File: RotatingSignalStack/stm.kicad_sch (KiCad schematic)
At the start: 17 parts, among them IC2 STM32H562RIT6, J2 Conn_01x04, SW1 SW_Push, SW2 Boot Switch

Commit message: more layout
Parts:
- C12, C13, C19, C20, C30, C31, C32, C33, C34, C35, C4: footprint Capacitor_SMD:C_0603_1608Metric_Pad1.08x0.95mm_HandSolder -> Capacitor_SMD:C_0402_1005Metric_Pad0.74x0.62mm_HandSolder
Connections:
- net VCAP1: no longer C32.2, IC2.62 (VCAP_2)
- new net VCAP2: C32.2, IC2.62 (VCAP_2)
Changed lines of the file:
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@@
 	)
 	(junction
-		(at 140.97 24.13)
-		(diameter 0)
-		(color 0 0 0 0)
-	)
-	(junction
 		(at 209.55 49.53)
 		(diameter 0)
@@
 	)
 	(junction
-		(at 140.97 27.94)
-		(diameter 0)
-		(color 0 0 0 0)
-	)
-	(junction
 		(at 238.76 49.53)
 		(diameter 0)
@@
 	(wire
 		(pts
-			(xy 140.97 24.13) (xy 140.97 27.94)
+			(xy 140.97 24.13) (xy 140.97 33.02)
 		)
 		(stroke
@@
 	(wire
 		(pts
-			(xy 154.94 27.94) (xy 140.97 27.94)
-		)
-		(stroke
-			(width 0)
-			(type default)
-		)
-	)
-	(wire
-		(pts
 			(xy 36.83 129.54) (xy 59.69 129.54)
 		)
@@
 	(wire
 		(pts
+			(xy 96.52 144.78) (xy 96.52 154.94)
+		)
+		(stroke
+			(width 0)
+			(type default)
+		)
+	)
+	(wire
+		(pts
 			(xy 208.28 27.94) (xy 209.55 27.94)
 		)
@@
 	(wire
 		(pts
-			(xy 140.97 20.32) (xy 140.97 24.13)
-		)
-		(stroke
-			(width 0)
-			(type default)
-		)
-	)
-	(wire
-		(pts
 			(xy 198.12 96.52) (xy 200.66 96.52)
 		)
@@
 	(wire
 		(pts
-			(xy 140.97 27.94) (xy 140.97 33.02)
-		)
-		(stroke
-			(width 0)
-			(type default)
-		)
-	)
-	(wire
-		(pts
-			(xy 140.97 20.32) (xy 137.16 20.32)
+			(xy 137.16 20.32) (xy 154.94 20.32)
 		)
 		(stroke
@@
 	(wire
 		(pts
-			(xy 154.94 33.02) (xy 154.94 27.94)
+			(xy 154.94 20.32) (xy 154.94 33.02)
 		)
 		(stroke
@@
 		)
 	)
-	(global_label "VSS_1"
-		(shape bidirectional)
-		(at 96.52 144.78 270)
-		(fields_autoplaced yes)
-		(effects
-			(font
-				(size 1.27 1.27)
-			)
-			(justify right)
-		)
-		(property "Intersheetrefs" "${INTERSHEET_REFS}"
-			(at 96.52 154.5612 90)
-			(effects
-				(font
-					(size 1.27 1.27)
-				)
-				(justify right)
-				(hide yes)
-			)
-		)
-	)
 	(global_label "VSS_2"
 		(shape bidirectional)
@@
 			)
 		)
-		(property "Footprint" "Capacitor_SMD:C_0603_1608Metric_Pad1.08x0.95mm_HandSolder"
+		(property "Footprint" "Capacitor_SMD:C_0402_1005Metric_Pad0.74x0.62mm_HandSolder"
 			(at 252.4252 81.28 0)
 			(effects
@@
 			)
 		)
-		(property "Footprint" "Capacitor_SMD:C_0603_1608Metric_Pad1.08x0.95mm_HandSolder"
+		(property "Footprint" "Capacitor_SMD:C_0402_1005Metric_Pad0.74x0.62mm_HandSolder"
 			(at 267.6652 110.49 0)
 			(effects
@@
 			)
 		)
-		(property "Footprint" "Capacitor_SMD:C_0603_1608Metric_Pad1.08x0.95mm_HandSolder"
+		(property "Footprint" "Capacitor_SMD:C_0402_1005Metric_Pad0.74x0.62mm_HandSolder"
 			(at 267.6652 81.28 0)
 			(effects
@@
 			)
 		)
-		(property "Footprint" "Capacitor_SMD:C_0603_1608Metric_Pad1.08x0.95mm_HandSolder"
+		(property "Footprint" "Capacitor_SMD:C_0402_1005Metric_Pad0.74x0.62mm_HandSolder"
 			(at 140.0048 33.02 0)
 			(effects
@@
 			)
 		)
-		(property "Footprint" "Capacitor_SMD:C_0603_1608Metric_Pad1.08x0.95mm_HandSolder"
+		(property "Footprint" "Capacitor_SMD:C_0402_1005Metric_Pad0.74x0.62mm_HandSolder"
 			(at 25.0952 124.46 0)
 			(effects
@@
 			)
 		)
-		(property "Footprint" "Capacitor_SMD:C_0603_1608Metric_Pad1.08x0.95mm_HandSolder"
+		(property "Footprint" "Capacitor_SMD:C_0402_1005Metric_Pad0.74x0.62mm_HandSolder"
 			(at 225.7552 45.72 0)
 			(effects
@@
 			)
 		)
-		(property "Footprint" "Capacitor_SMD:C_0603_1608Metric_Pad1.08x0.95mm_HandSolder"
+		(property "Footprint" "Capacitor_SMD:C_0402_1005Metric_Pad0.74x0.62mm_HandSolder"
 			(at 267.6652 45.72 0)
 			(effects
@@
 	(symbol
 		(lib_id "power:GND")
+		(at 96.52 154.94 0)
+		(unit 1)
+		(exclude_from_sim no)
+		(in_bom yes)
+		(on_board yes)
+		(dnp no)
+		(fields_autoplaced yes)
+		(property "Reference" "#PWR026"
+			(at 96.52 161.29 0)
+			(effects
+				(font
+					(size 1.27 1.27)
+				)
+				(hide yes)
+			)
+		)
+		(property "Value" "GND"
+			(at 96.52 160.02 0)
+			(effects
+				(font
+					(size 1.27 1.27)
+				)
+			)
+		)
+		(property "Footprint" ""
+			(at 96.52 154.94 0)
+			(effects
+				(font
+					(size 1.27 1.27)
+				)
+				(hide yes)
+			)
+		)
+		(property "Datasheet" ""
+			(at 96.52 154.94 0)
+			(effects
+				(font
+					(size 1.27 1.27)
+				)
+				(hide yes)
+			)
+		)
+		(property "Description" "Power symbol creates a global label with name \"GND\" , ground"
+			(at 96.52 154.94 0)
+			(effects
+				(font
+					(size 1.27 1.27)
+				)
+				(hide yes)
+			)
+		)
+		(pin "1"
+		)
+		(instances
+			(project ""
+				(path "/fbbbfa89-3c28-4cf8-856b-66ca7308742c/85f5c4be-2744-4dc6-8792-10e4391fb2cb"
+					(reference "#PWR026")
+					(unit 1)
+				)
+			)
+		)
+	)
+	(symbol
+		(lib_id "power:GND")
 		(at 181.61 38.1 0)
 		(unit 1)
@@
 			)
 		)
-		(property "Footprint" "Capacitor_SMD:C_0603_1608Metric_Pad1.08x0.95mm_HandSolder"
+		(property "Footprint" "Capacitor_SMD:C_0402_1005Metric_Pad0.74x0.62mm_HandSolder"
 			(at 253.6952 45.72 0)
 			(effects
@@
 			)
 		)
-		(property "Footprint" "Capacitor_SMD:C_0603_1608Metric_Pad1.08x0.95mm_HandSolder"
+		(property "Footprint" "Capacitor_SMD:C_0402_1005Metric_Pad0.74x0.62mm_HandSolder"
 			(at 210.5152 45.72 0)
 			(effects
@@
 			)
 		)
-		(property "Footprint" "Capacitor_SMD:C_0603_1608Metric_Pad1.08x0.95mm_HandSolder"
+		(property "Footprint" "Capacitor_SMD:C_0402_1005Metric_Pad0.74x0.62mm_HandSolder"
 			(at 239.7252 45.72 0)
 			(effects
@@
 			)
 		)
-		(property "Footprint" "Capacitor_SMD:C_0603_1608Metric_Pad1.08x0.95mm_HandSolder"
+		(property "Footprint" "Capacitor_SMD:C_0402_1005Metric_Pad0.74x0.62mm_HandSolder"
 			(at 153.9748 33.02 0)
 			(effects

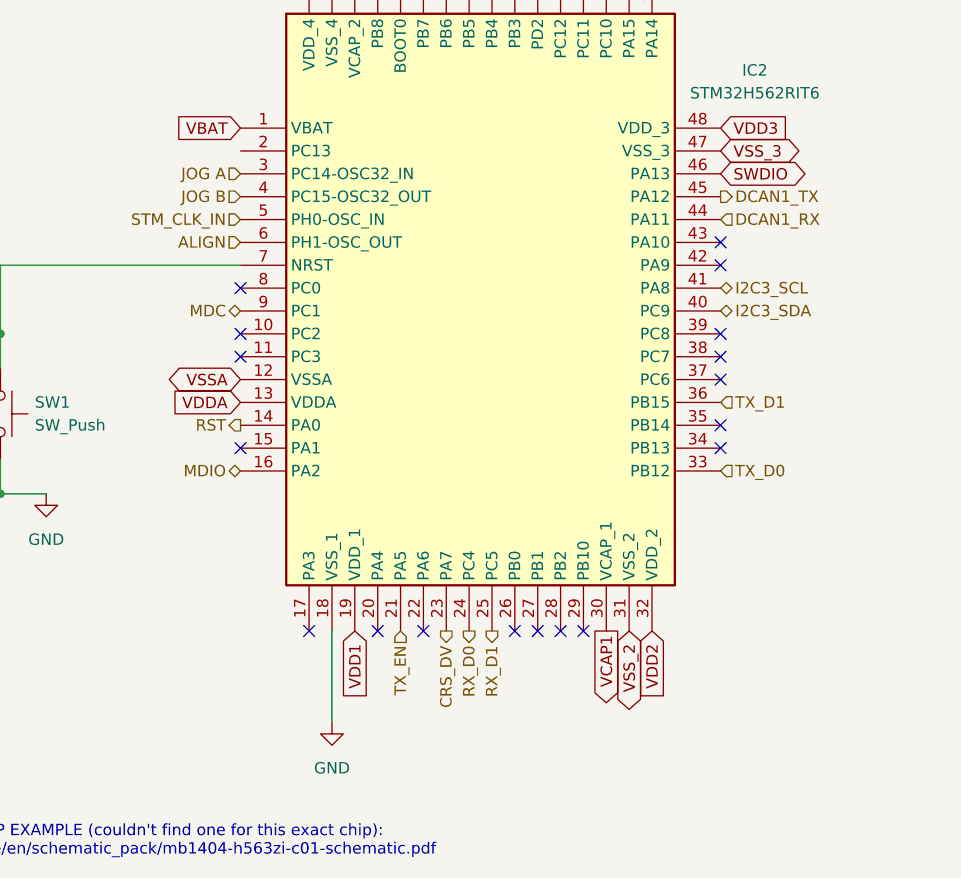
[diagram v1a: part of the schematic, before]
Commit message: Finished traces, added silkscreen
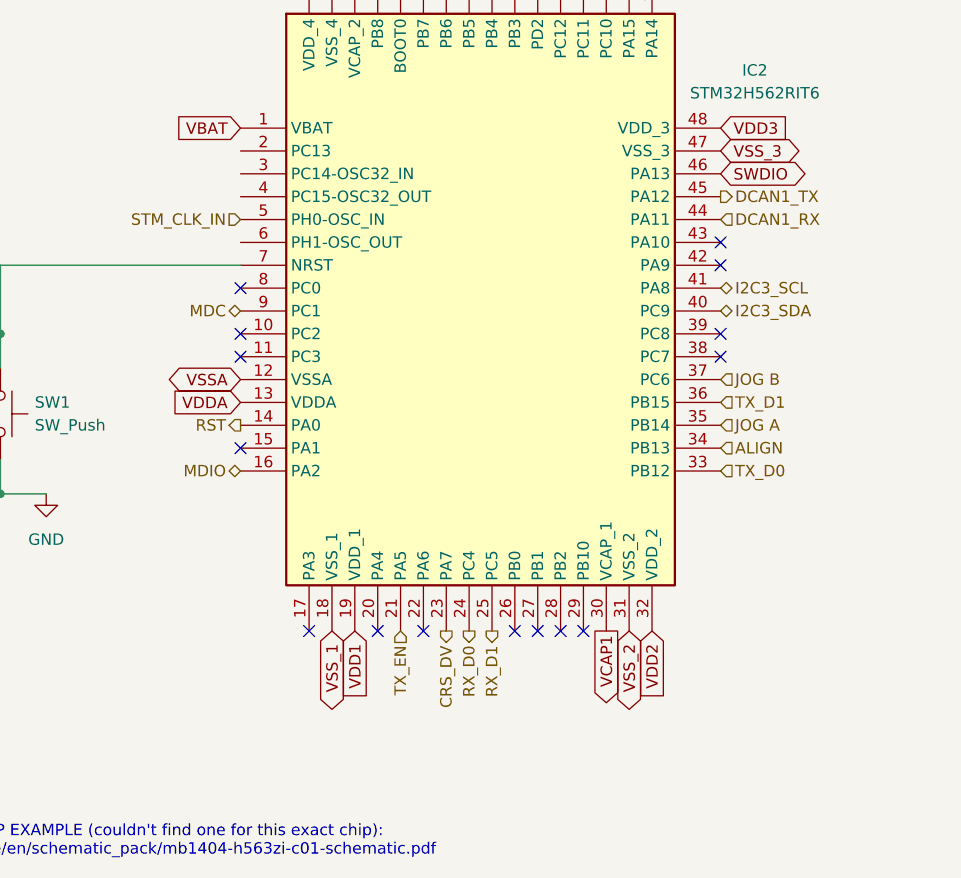
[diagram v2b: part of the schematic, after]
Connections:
- net ALIGN: now also IC2.34 (PB13); no longer IC2.6 (PH1-OSC_OUT)
- net JOG A: now also IC2.35 (PB14); no longer IC2.3 (PC14-OSC32_IN)
- net JOG B: now also IC2.37 (PC6); no longer IC2.4 (PC15-OSC32_OUT)
- no-connect marks 26 -> 23
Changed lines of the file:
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@@
-	)
-	(no_connect
-		(at 139.7 116.84)
 	)
 	(no_connect
@@
 	)
 	(no_connect
-		(at 139.7 121.92)
-	)
-	(no_connect
 		(at 116.84 144.78)
 	)
@@
 		(at 129.54 71.12)
 	)
-	(no_connect
-		(at 139.7 124.46)
-	)
 	(wire
 		(pts
@@
 		(pts
 			(xy 208.28 31.75) (xy 209.55 31.75)
-		)
-		(stroke
-			(width 0)
-			(type default)
-		)
-	)
-	(wire
-		(pts
-			(xy 96.52 144.78) (xy 96.52 154.94)
 		)
 		(stroke
@@
 		)
 	)
+	(global_label "VSS_1"
+		(shape bidirectional)
+		(at 96.52 144.78 270)
+		(fields_autoplaced yes)
+		(effects
+			(font
+				(size 1.27 1.27)
+			)
+			(justify right)
+		)
+		(property "Intersheetrefs" "${INTERSHEET_REFS}"
+			(at 96.52 154.5612 90)
+			(effects
+				(font
+					(size 1.27 1.27)
+				)
+				(justify right)
+				(hide yes)
+			)
+		)
+	)
 	(global_label "SWDIO"
 		(shape bidirectional)
@@
 		)
 	)
-	(hierarchical_label "ALIGN"
+	(hierarchical_label "JOG A"
 		(shape input)
-		(at 86.36 101.6 180)
-		(effects
-			(font
-				(size 1.27 1.27)
-			)
-			(justify right)
+		(at 139.7 121.92 0)
+		(effects
+			(font
+				(size 1.27 1.27)
+			)
+			(justify left)
 		)
 	)
@@
 		)
 	)
+	(hierarchical_label "JOG B"
+		(shape input)
+		(at 139.7 116.84 0)
+		(effects
+			(font
+				(size 1.27 1.27)
+			)
+			(justify left)
+		)
+	)
 	(hierarchical_label "I2C3_SCL"
 		(shape bidirectional)
@@
 		)
 	)
-	(hierarchical_label "JOG A"
+	(hierarchical_label "ALIGN"
 		(shape input)
-		(at 86.36 93.98 180)
-		(effects
-			(font
-				(size 1.27 1.27)
-			)
-			(justify right)
+		(at 139.7 124.46 0)
+		(effects
+			(font
+				(size 1.27 1.27)
+			)
+			(justify left)
 		)
 	)
@@
 		(shape bidirectional)
 		(at 86.36 127 180)
-		(effects
-			(font
-				(size 1.27 1.27)
-			)
-			(justify right)
-		)
-	)
-	(hierarchical_label "JOG B"
-		(shape input)
-		(at 86.36 96.52 180)
 		(effects
 			(font
@@
 					(unit 1)
 				)
-			)
-		)
-	)
-	(symbol
-		(lib_id "power:GND")
-		(at 96.52 154.94 0)
-		(unit 1)
-		(exclude_from_sim no)
-		(in_bom yes)
-		(on_board yes)
-		(dnp no)
-		(fields_autoplaced yes)
-		(property "Reference" "#PWR026"
-			(at 96.52 161.29 0)
-			(effects
-				(font
-					(size 1.27 1.27)
-				)
-				(hide yes)
-			)
-		)
-		(property "Value" "GND"
-			(at 96.52 160.02 0)
-			(effects
-				(font
-					(size 1.27 1.27)
-				)
-			)
-		)
-		(property "Footprint" ""
-			(at 96.52 154.94 0)
-			(effects
-				(font
-					(size 1.27 1.27)
-				)
-				(hide yes)
-			)
-		)
-		(property "Datasheet" ""
-			(at 96.52 154.94 0)
-			(effects
-				(font
-					(size 1.27 1.27)
-				)
-				(hide yes)
-			)
-		)
-		(property "Description" "Power symbol creates a global label with name \"GND\" , ground"
-			(at 96.52 154.94 0)
-			(effects
-				(font
-					(size 1.27 1.27)
-				)
-				(hide yes)
-			)
-		)
-		(pin "1"
-		)
-		(instances
-			(project ""
-				(path "/fbbbfa89-3c28-4cf8-856b-66ca7308742c/85f5c4be-2744-4dc6-8792-10e4391fb2cb"
-					(reference "#PWR026")
-					(unit 1)
-				)

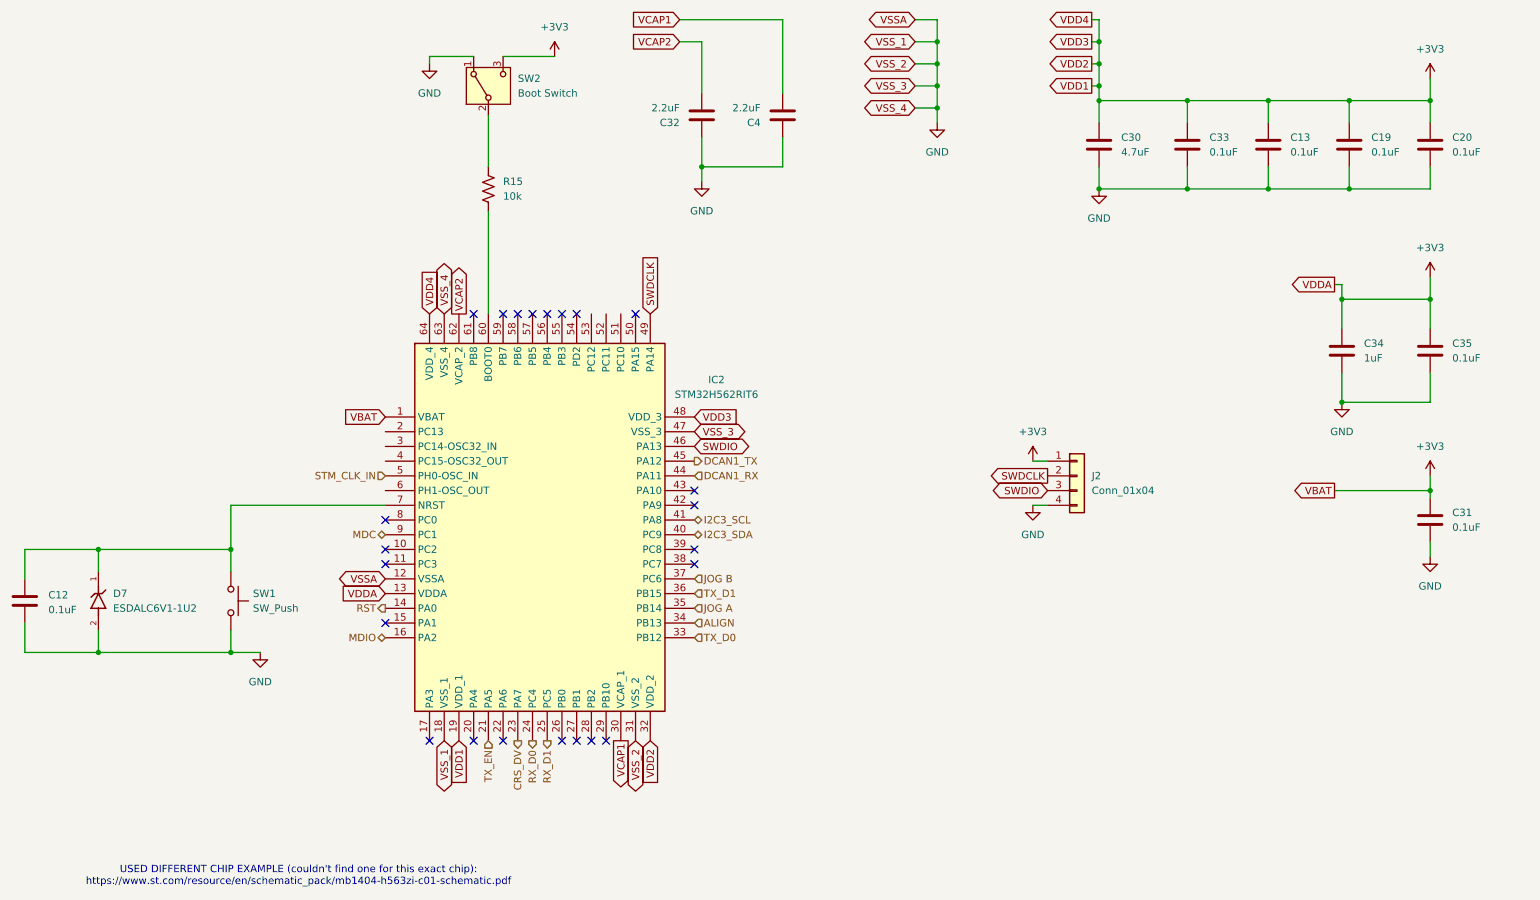
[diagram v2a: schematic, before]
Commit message: More changes
compass and oki conn and 6 pin conn with the old DIR/EN/STP/COM, fix trace length, under 50 mil Vbus, tree branch
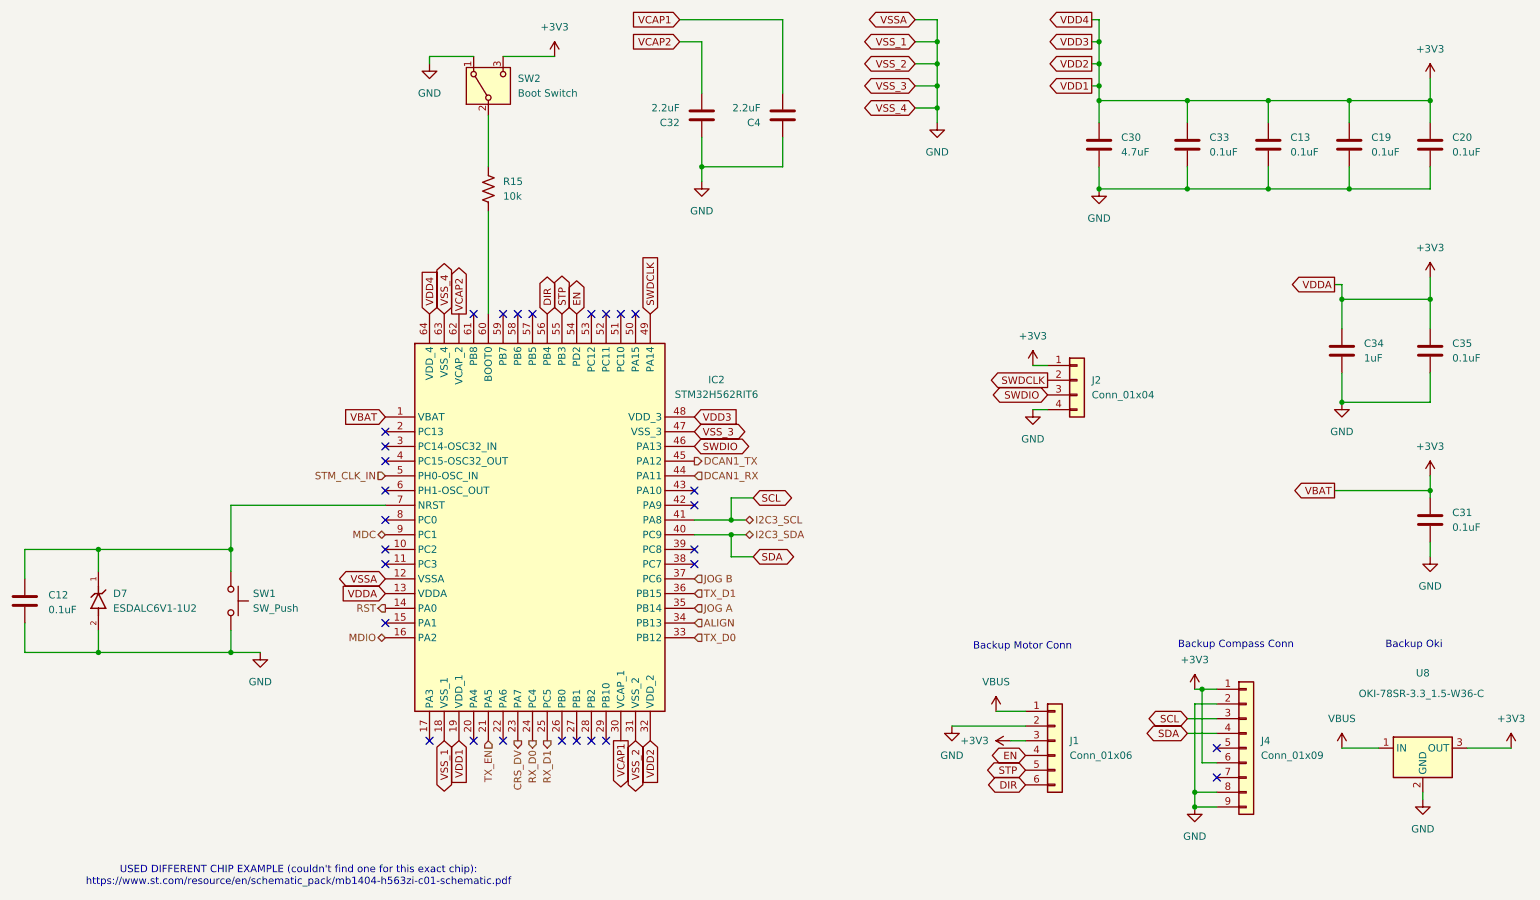
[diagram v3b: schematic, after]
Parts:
- added J1: Conn_01x06, Connector_PinSocket_2.54mm:PinSocket_1x06_P2.54mm_Vertical, symbol Connector_Generic:Conn_01x06
- added J4: Conn_01x09, Connector_PinSocket_2.54mm:PinSocket_1x09_P2.54mm_Vertical, symbol Connector_Generic:Conn_01x09
- added U8: OKI-78SR-3.3_1.5-W36-C, Converter_DCDC:Converter_DCDC_Murata_OKI-78SR_Vertical, symbol Converter_DCDC:OKI-78SR-3.3_1.5-W36-C
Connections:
- net +3V3: now also J1.3 (Pin_3), J4.1 (Pin_1), J4.6 (Pin_6), U8.3 (OUT)
- net GND: now also J1.2 (Pin_2), J4.2 (Pin_2), J4.8 (Pin_8), J4.9 (Pin_9), U8.2 (GND)
- net EN: now reaches IC2.54 (PD2)
- net EN: now also J1.4 (Pin_4)
- net STP: now reaches IC2.55 (PB3)
- net STP: now also J1.5 (Pin_5)
- net DIR: now reaches IC2.56 (PB4)
- net DIR: now also J1.6 (Pin_6)
- net I2C3_SCL renamed SCL
- net SCL: now also J4.3 (Pin_3)
- net I2C3_SDA renamed SDA
- net SDA: now also J4.4 (Pin_4)
- new net VBUS: J1.1 (Pin_1), U8.1 (IN)
- no-connect marks 23 -> 29
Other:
- note added: "Backup Compass Conn"
- note added: "Backup Motor Conn"
- note added: "Backup Oki"
- moved on the sheet: J2

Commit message: Added ground edges and fixed capacitors and layout issues
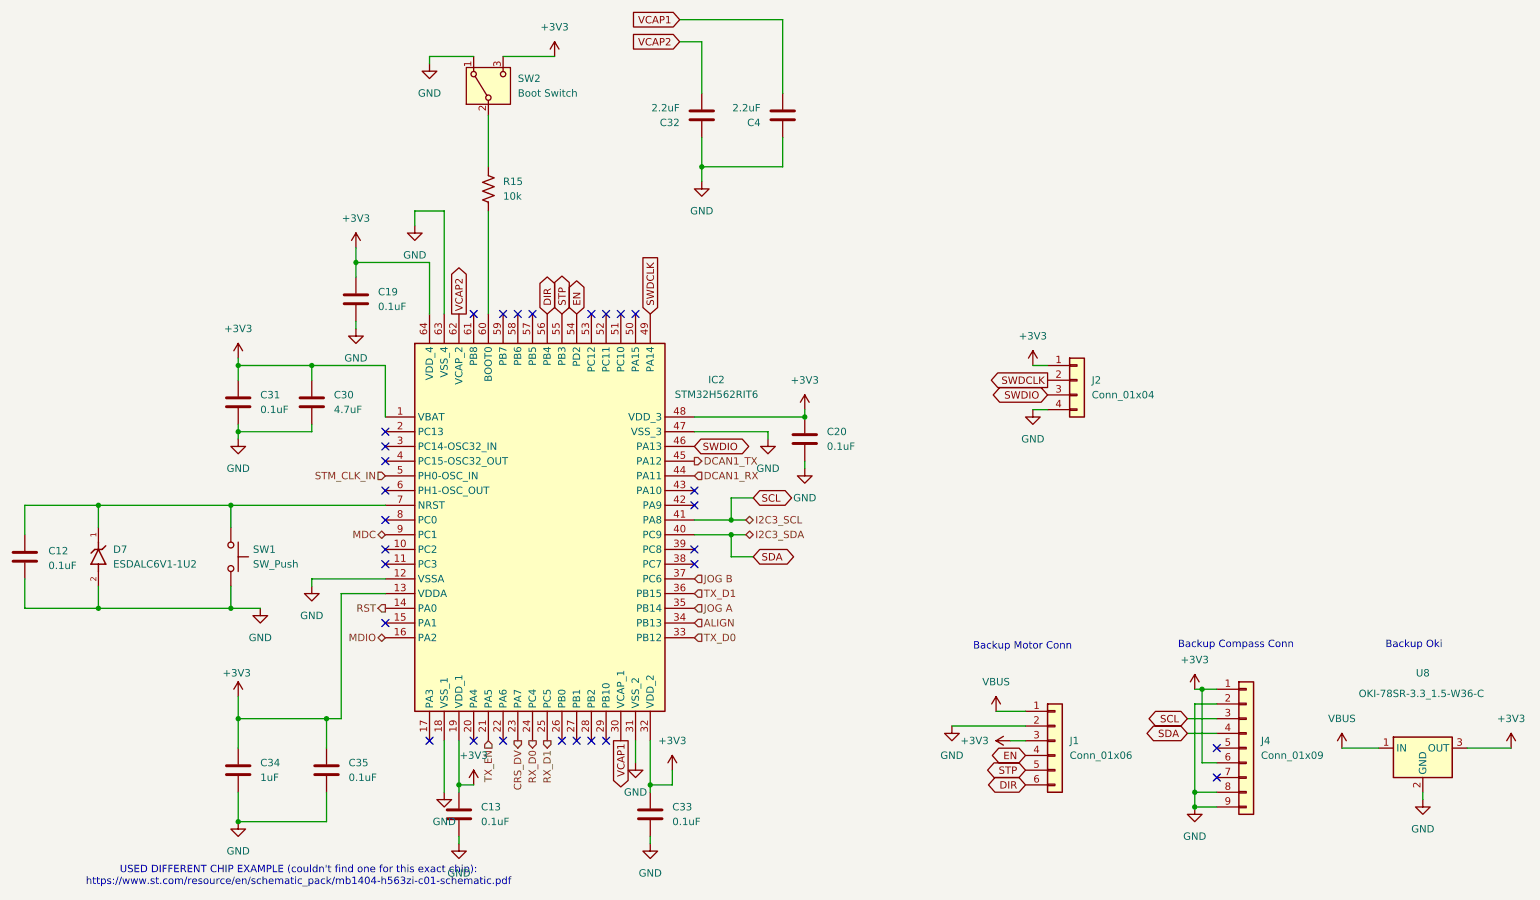
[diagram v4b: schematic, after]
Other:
- moved on the sheet: C12, C13, C19, C20, C30, C31, C33, C34, C35, D7, SW1
